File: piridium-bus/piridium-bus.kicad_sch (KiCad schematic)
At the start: 87 parts, among them J1 EPS, J2 INHIBITS, J3 MODEM UART, J4 ANT, J5 PAYLOAD, Q1 DMP3015LSSQ, Q2 Si4186DY, Q3 DMP3015LSSQ, Q4 Si4186DY, Q5 DMP3015LSSQ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

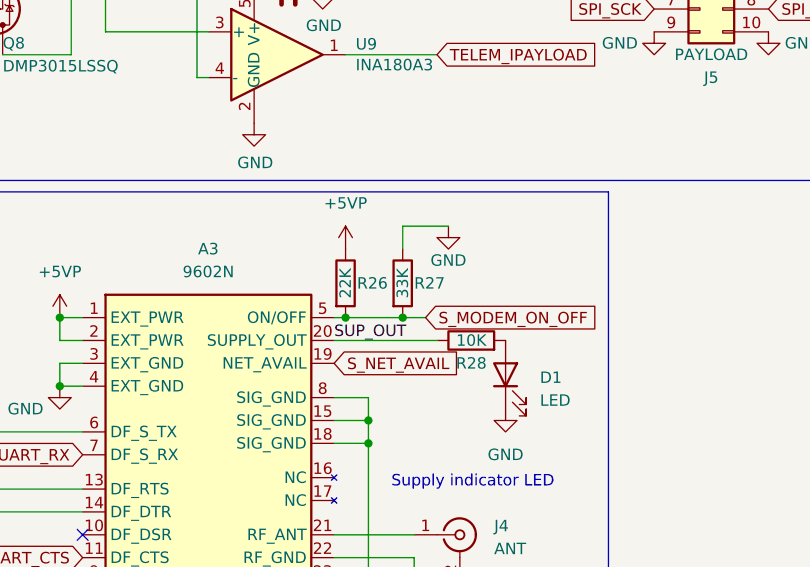
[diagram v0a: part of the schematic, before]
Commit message: pull down on/off instead of up
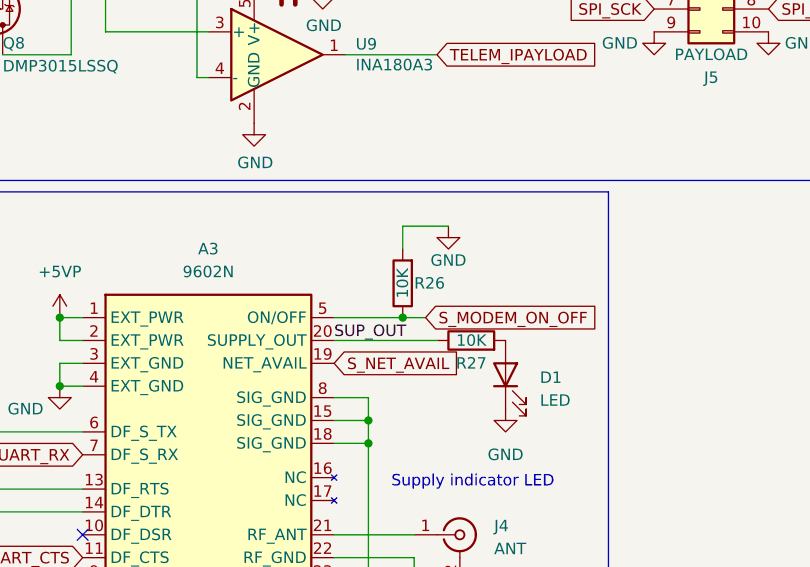
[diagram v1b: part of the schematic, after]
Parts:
- removed R27: 33K, Resistor_SMD:R_1206_3216Metric, symbol Device:R
- R26: value 22K -> 10K; footprint Resistor_SMD:R_1206_3216Metric -> Resistor_SMD:R_0805_2012Metric
- renumbered R28 to R27
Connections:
- net +5VP: no longer R26.1
- net GND: now also R26.2
- net S_MODEM_ON_OFF: now also R26.1; no longer R26.2

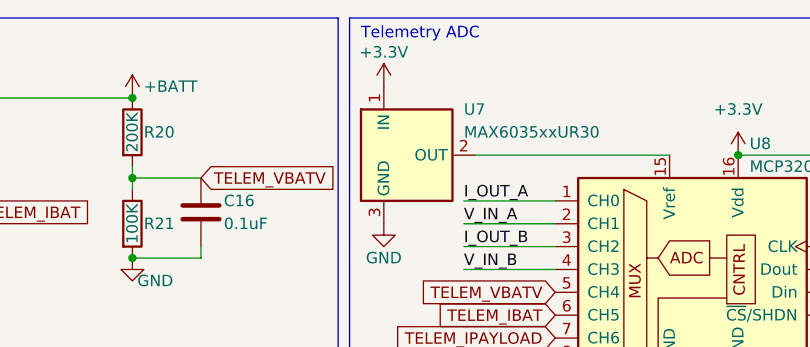
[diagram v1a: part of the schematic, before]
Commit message: fix max6035 dropout
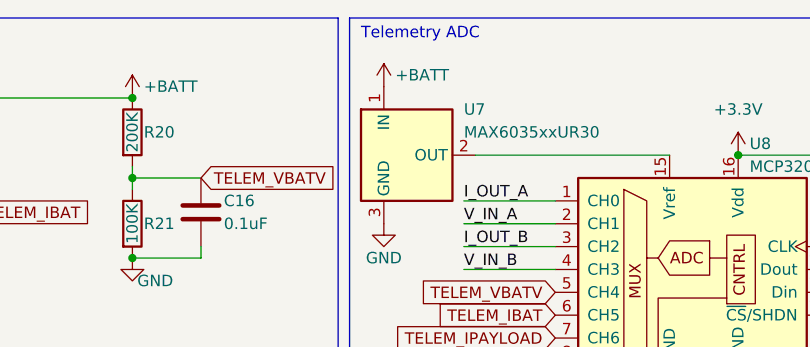
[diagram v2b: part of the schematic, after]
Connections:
- net +3.3V: no longer U7.1 (IN)
- net +BATT: now also U7.1 (IN)
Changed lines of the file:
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@@
+    (pin "1")
+  )
+  (symbol (lib_id "power:+BATT") (at 208.28 20.32 0) (unit 1)
+    (in_bom yes) (on_board yes)
+    (property "Reference" "#PWR?" (id 0) (at 208.28 24.13 0)
+      (effects (font (size 1.27 1.27)) hide)
+    )
+    (property "Value" "+BATT" (id 1) (at 209.55 19.05 0)
+      (effects (font (size 1.27 1.27)) (justify left))
+    )
+    (property "Footprint" "" (id 2) (at 208.28 20.32 0)
+      (effects (font (size 1.27 1.27)) hide)
+    )
+    (property "Datasheet" "" (id 3) (at 208.28 20.32 0)
+      (effects (font (size 1.27 1.27)) hide)
+    )
     (pin "1")
   )
@@
     (pin "1")
     (pin "2")
-  )
-  (symbol (lib_id "power:+3.3V") (at 208.28 20.32 0) (unit 1)
-    (in_bom yes) (on_board yes)
-    (property "Reference" "#PWR031" (id 0) (at 208.28 24.13 0)
-      (effects (font (size 1.27 1.27)) hide)
-    )
-    (property "Value" "+3.3V" (id 1) (at 208.28 16.51 0))
-    (property "Footprint" "" (id 2) (at 208.28 20.32 0)
-      (effects (font (size 1.27 1.27)) hide)
-    )
-    (property "Datasheet" "" (id 3) (at 208.28 20.32 0)
-      (effects (font (size 1.27 1.27)) hide)
-    )
-    (pin "1")
   )
   (symbol (lib_id "Transistor_FET:IRF7404") (at 102.87 24.13 270) (mirror x) (unit 1)
@@
       (reference "#PWR030") (unit 1) (value "GND") (footprint "")
     )
-    (path "/4304edc3-4a15-4a04-95b2-40c12ad316a4"
-      (reference "#PWR031") (unit 1) (value "+3.3V") (footprint "")
-    )
     (path "/00b4f894-fd03-4264-a14f-fc8743af3471"
       (reference "#PWR032") (unit 1) (value "GND") (footprint "")
@@
       (reference "#PWR074") (unit 1) (value "GND") (footprint "")
     )
+    (path "/0572d3b7-c872-41b1-b65f-ce6e9b18c5ab"
+      (reference "#PWR?") (unit 1) (value "+BATT") (footprint "")
+    )
     (path "/dee1721c-7498-4aa5-ba4d-8809f87db910"
